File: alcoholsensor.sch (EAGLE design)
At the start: 23 parts, among them IC2 7805TV

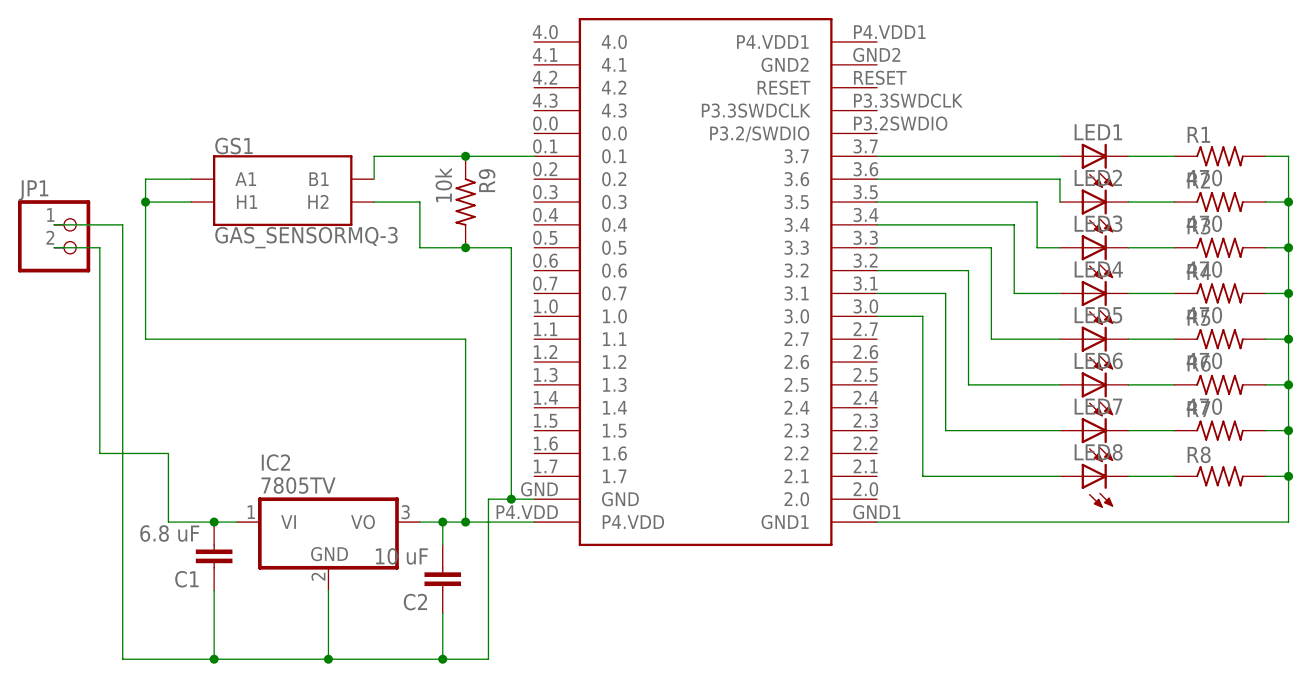
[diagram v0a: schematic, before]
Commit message: Improved design (made smaller)
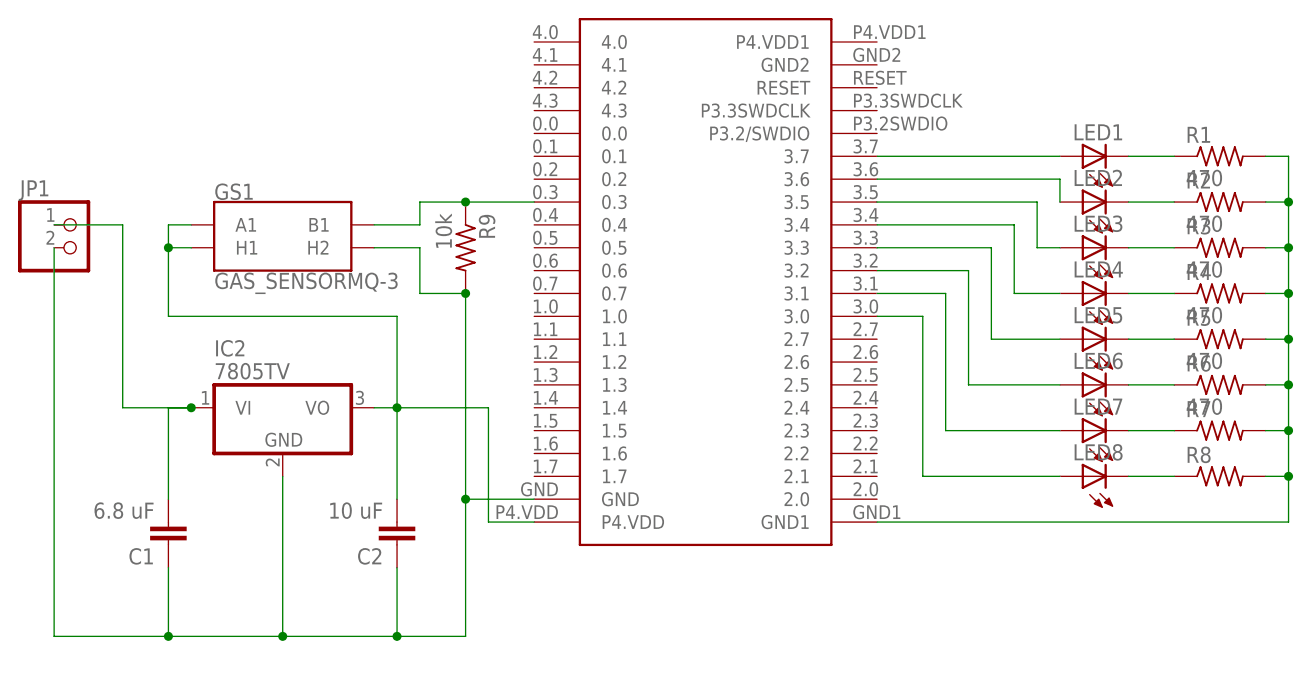
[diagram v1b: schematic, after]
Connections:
- removed net N$20 (its old number): GS1.B1, R9.1, U$1.0.1
- new net N$18: C1.2, IC2.VI, JP1.1
- net N$21: now also GS1.B1, R9.1, U$1.0.3; no longer C1.2, IC2.VI, JP1.2
- net N$22: now also JP1.2; no longer JP1.1
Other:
- moved on the sheet: C1, C2, GS1, IC2, R9
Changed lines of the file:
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@@
 <instance part="R7" gate="G$1" x="147.32" y="27.94"/>
 <instance part="R8" gate="G$1" x="147.32" y="22.86"/>
-<instance part="R9" gate="G$1" x="63.5" y="53.34" rot="R270"/>
+<instance part="R9" gate="G$1" x="63.5" y="48.26" rot="R270"/>
 <instance part="JP1" gate="G$1" x="20.32" y="48.26"/>
-<instance part="IC2" gate="A1" x="48.26" y="17.78"/>
-<instance part="C1" gate="G$1" x="35.56" y="12.7" rot="R180"/>
-<instance part="C2" gate="G$1" x="60.96" y="10.16" rot="R180"/>
-<instance part="GS1" gate="G$1" x="43.18" y="53.34"/>
+<instance part="IC2" gate="A1" x="43.18" y="30.48"/>
+<instance part="C1" gate="G$1" x="30.48" y="15.24" rot="R180"/>
+<instance part="C2" gate="G$1" x="55.88" y="15.24" rot="R180"/>
+<instance part="GS1" gate="G$1" x="43.18" y="48.26"/>
 </instances>
 <busses>
@@
 <net name="N$18" class="0">
 <segment>
+<pinref part="JP1" gate="G$1" pin="1"/>
+<wire x1="17.78" y1="50.8" x2="25.4" y2="50.8" width="0.1524" layer="91"/>
+<wire x1="25.4" y1="50.8" x2="25.4" y2="30.48" width="0.1524" layer="91"/>
+<pinref part="IC2" gate="A1" pin="VI"/>
+<wire x1="25.4" y1="30.48" x2="33.02" y2="30.48" width="0.1524" layer="91"/>
+<pinref part="C1" gate="G$1" pin="2"/>
+<wire x1="33.02" y1="30.48" x2="30.48" y2="30.48" width="0.1524" layer="91"/>
+<wire x1="30.48" y1="30.48" x2="30.48" y2="20.32" width="0.1524" layer="91"/>
+<junction x="33.02" y="30.48"/>
+</segment>
+</net>
+<net name="N$20" class="0">
+<segment>
+<pinref part="C2" gate="G$1" pin="2"/>
+<wire x1="55.88" y1="20.32" x2="55.88" y2="30.48" width="0.1524" layer="91"/>
+<pinref part="IC2" gate="A1" pin="VO"/>
+<wire x1="55.88" y1="30.48" x2="53.34" y2="30.48" width="0.1524" layer="91"/>
+<wire x1="66.04" y1="30.48" x2="66.04" y2="17.78" width="0.1524" layer="91"/>
+<junction x="55.88" y="30.48"/>
 <pinref part="U$1" gate="G$1" pin="P4.VDD"/>
-<wire x1="58.42" y1="17.78" x2="60.96" y2="17.78" width="0.1524" layer="91"/>
-<wire x1="60.96" y1="17.78" x2="63.5" y2="17.78" width="0.1524" layer="91"/>
-<wire x1="63.5" y1="17.78" x2="71.12" y2="17.78" width="0.1524" layer="91"/>
-<wire x1="63.5" y1="17.78" x2="63.5" y2="38.1" width="0.1524" layer="91"/>
-<junction x="63.5" y="17.78"/>
-<wire x1="63.5" y1="38.1" x2="27.94" y2="38.1" width="0.1524" layer="91"/>
-<wire x1="27.94" y1="38.1" x2="27.94" y2="53.34" width="0.1524" layer="91"/>
-<pinref part="IC2" gate="A1" pin="VO"/>
-<pinref part="C2" gate="G$1" pin="2"/>
-<wire x1="27.94" y1="53.34" x2="27.94" y2="55.88" width="0.1524" layer="91"/>
-<wire x1="60.96" y1="15.24" x2="60.96" y2="17.78" width="0.1524" layer="91"/>
-<junction x="60.96" y="17.78"/>
+<wire x1="66.04" y1="17.78" x2="71.12" y2="17.78" width="0.1524" layer="91"/>
+<wire x1="66.04" y1="30.48" x2="55.88" y2="30.48" width="0.1524" layer="91"/>
+<wire x1="55.88" y1="30.48" x2="55.88" y2="40.64" width="0.1524" layer="91"/>
+<wire x1="55.88" y1="40.64" x2="30.48" y2="40.64" width="0.1524" layer="91"/>
+<wire x1="30.48" y1="40.64" x2="30.48" y2="48.26" width="0.1524" layer="91"/>
+<pinref part="GS1" gate="G$1" pin="H1"/>
+<wire x1="30.48" y1="48.26" x2="33.02" y2="48.26" width="0.1524" layer="91"/>
 <pinref part="GS1" gate="G$1" pin="A1"/>
-<wire x1="27.94" y1="55.88" x2="33.02" y2="55.88" width="0.1524" layer="91"/>
-<pinref part="GS1" gate="G$1" pin="H1"/>
-<wire x1="27.94" y1="53.34" x2="33.02" y2="53.34" width="0.1524" layer="91"/>
-<junction x="27.94" y="53.34"/>
-</segment>
-</net>
-<net name="N$20" class="0">
-<segment>
+<wire x1="33.02" y1="50.8" x2="30.48" y2="50.8" width="0.1524" layer="91"/>
+<wire x1="30.48" y1="50.8" x2="30.48" y2="48.26" width="0.1524" layer="91"/>
+<junction x="30.48" y="48.26"/>
+</segment>
+</net>
+<net name="N$21" class="0">
+<segment>
+<pinref part="GS1" gate="G$1" pin="B1"/>
+<wire x1="53.34" y1="50.8" x2="58.42" y2="50.8" width="0.1524" layer="91"/>
+<wire x1="58.42" y1="50.8" x2="58.42" y2="53.34" width="0.1524" layer="91"/>
 <pinref part="R9" gate="G$1" pin="1"/>
-<pinref part="U$1" gate="G$1" pin="0.1"/>
-<wire x1="63.5" y1="58.42" x2="71.12" y2="58.42" width="0.1524" layer="91"/>
-<pinref part="GS1" gate="G$1" pin="B1"/>
-<wire x1="53.34" y1="55.88" x2="53.34" y2="58.42" width="0.1524" layer="91"/>
-<wire x1="53.34" y1="58.42" x2="63.5" y2="58.42" width="0.1524" layer="91"/>
-<junction x="63.5" y="58.42"/>
-</segment>
-</net>
-<net name="N$21" class="0">
-<segment>
-<wire x1="30.48" y1="25.4" x2="30.48" y2="17.78" width="0.1524" layer="91"/>
+<wire x1="58.42" y1="53.34" x2="63.5" y2="53.34" width="0.1524" layer="91"/>
+<pinref part="U$1" gate="G$1" pin="0.3"/>
+<wire x1="63.5" y1="53.34" x2="71.12" y2="53.34" width="0.1524" layer="91"/>
+<junction x="63.5" y="53.34"/>
+</segment>
+</net>
+<net name="N$22" class="0">
+<segment>
+<pinref part="GS1" gate="G$1" pin="H2"/>
+<wire x1="53.34" y1="48.26" x2="58.42" y2="48.26" width="0.1524" layer="91"/>
+<wire x1="58.42" y1="48.26" x2="58.42" y2="43.18" width="0.1524" layer="91"/>
+<pinref part="R9" gate="G$1" pin="2"/>
+<wire x1="58.42" y1="43.18" x2="63.5" y2="43.18" width="0.1524" layer="91"/>
 <pinref part="JP1" gate="G$1" pin="2"/>
-<wire x1="17.78" y1="48.26" x2="22.86" y2="48.26" width="0.1524" layer="91"/>
-<wire x1="22.86" y1="48.26" x2="22.86" y2="25.4" width="0.1524" layer="91"/>
-<wire x1="22.86" y1="25.4" x2="30.48" y2="25.4" width="0.1524" layer="91"/>
-<pinref part="IC2" gate="A1" pin="VI"/>
-<pinref part="C1" gate="G$1" pin="2"/>
-<wire x1="38.1" y1="17.78" x2="35.56" y2="17.78" width="0.1524" layer="91"/>
-<wire x1="30.48" y1="17.78" x2="35.56" y2="17.78" width="0.1524" layer="91"/>
-<junction x="35.56" y="17.78"/>
-</segment>
-</net>
-<net name="N$22" class="0">
-<segment>
-<wire x1="48.26" y1="10.16" x2="48.26" y2="2.54" width="0.1524" layer="91"/>
-<wire x1="48.26" y1="2.54" x2="60.96" y2="2.54" width="0.1524" layer="91"/>
-<wire x1="60.96" y1="2.54" x2="66.04" y2="2.54" width="0.1524" layer="91"/>
-<wire x1="66.04" y1="2.54" x2="66.04" y2="20.32" width="0.1524" layer="91"/>
-<junction x="48.26" y="2.54"/>
+<wire x1="17.78" y1="48.26" x2="17.78" y2="5.08" width="0.1524" layer="91"/>
+<wire x1="17.78" y1="5.08" x2="30.48" y2="5.08" width="0.1524" layer="91"/>
+<pinref part="IC2" gate="A1" pin="GND"/>
+<wire x1="30.48" y1="5.08" x2="43.18" y2="5.08" width="0.1524" layer="91"/>
+<wire x1="43.18" y1="5.08" x2="43.18" y2="22.86" width="0.1524" layer="91"/>
+<pinref part="C1" gate="G$1" pin="1"/>
+<wire x1="30.48" y1="12.7" x2="30.48" y2="5.08" width="0.1524" layer="91"/>
+<junction x="30.48" y="5.08"/>
+<pinref part="C2" gate="G$1" pin="1"/>
+<wire x1="55.88" y1="12.7" x2="55.88" y2="5.08" width="0.1524" layer="91"/>
+<wire x1="55.88" y1="5.08" x2="43.18" y2="5.08" width="0.1524" layer="91"/>
+<junction x="43.18" y="5.08"/>
+<wire x1="55.88" y1="5.08" x2="63.5" y2="5.08" width="0.1524" layer="91"/>
+<wire x1="63.5" y1="5.08" x2="63.5" y2="20.32" width="0.1524" layer="91"/>
+<junction x="55.88" y="5.08"/>
 <pinref part="U$1" gate="G$1" pin="GND"/>
-<wire x1="66.04" y1="20.32" x2="68.58" y2="20.32" width="0.1524" layer="91"/>
-<wire x1="68.58" y1="20.32" x2="71.12" y2="20.32" width="0.1524" layer="91"/>
-<pinref part="R9" gate="G$1" pin="2"/>
-<wire x1="58.42" y1="48.26" x2="63.5" y2="48.26" width="0.1524" layer="91"/>
-<wire x1="63.5" y1="48.26" x2="68.58" y2="48.26" width="0.1524" layer="91"/>
-<wire x1="68.58" y1="48.26" x2="68.58" y2="20.32" width="0.1524" layer="91"/>
-<junction x="63.5" y="48.26"/>
-<junction x="68.58" y="20.32"/>
-<wire x1="48.26" y1="2.54" x2="35.56" y2="2.54" width="0.1524" layer="91"/>
-<wire x1="35.56" y1="2.54" x2="25.4" y2="2.54" width="0.1524" layer="91"/>
-<wire x1="25.4" y1="2.54" x2="25.4" y2="50.8" width="0.1524" layer="91"/>
-<pinref part="JP1" gate="G$1" pin="1"/>
-<wire x1="25.4" y1="50.8" x2="17.78" y2="50.8" width="0.1524" layer="91"/>
-<pinref part="IC2" gate="A1" pin="GND"/>
-<pinref part="C1" gate="G$1" pin="1"/>
-<wire x1="35.56" y1="10.16" x2="35.56" y2="2.54" width="0.1524" layer="91"/>
-<junction x="35.56" y="2.54"/>
-<pinref part="C2" gate="G$1" pin="1"/>
-<wire x1="60.96" y1="7.62" x2="60.96" y2="2.54" width="0.1524" layer="91"/>
-<junction x="60.96" y="2.54"/>
-<pinref part="GS1" gate="G$1" pin="H2"/>
-<wire x1="53.34" y1="53.34" x2="58.42" y2="53.34" width="0.1524" layer="91"/>
-<wire x1="58.42" y1="53.34" x2="58.42" y2="48.26" width="0.1524" layer="91"/>
-</segment>
-</net>
+<wire x1="63.5" y1="20.32" x2="71.12" y2="20.32" width="0.1524" layer="91"/>
+<wire x1="63.5" y1="43.18" x2="63.5" y2="20.32" width="0.1524" layer="91"/>
+<junction x="63.5" y="43.18"/>
+<junction x="63.5" y="20.32"/>
+</segment>
+</net>

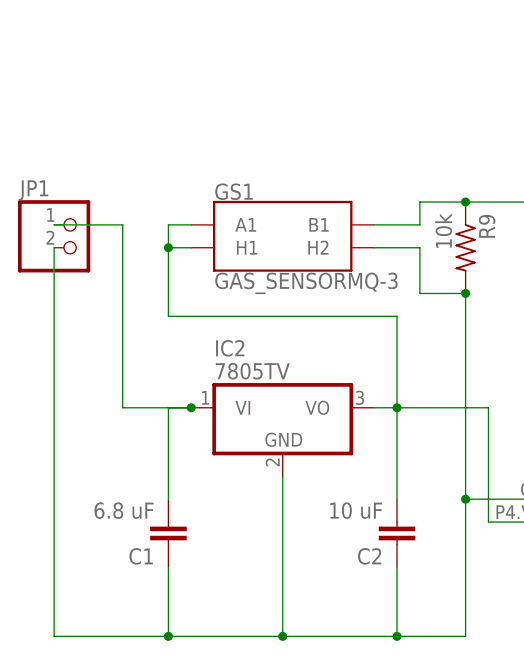
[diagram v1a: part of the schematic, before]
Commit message: Added pushbutton switch to control power source
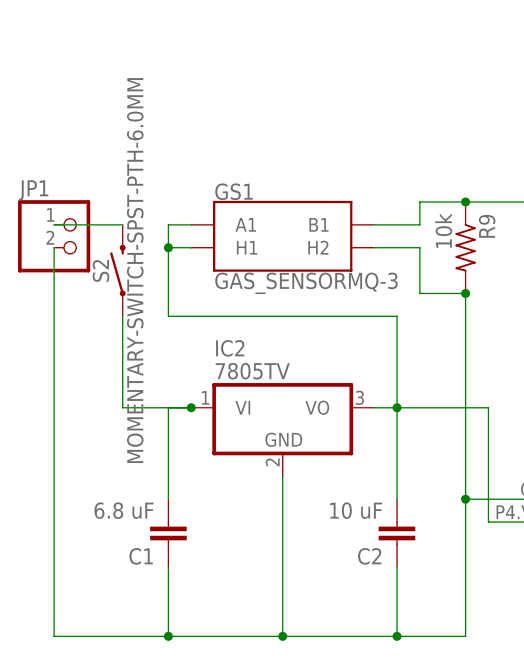
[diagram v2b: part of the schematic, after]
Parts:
- added S2: MOMENTARY-SWITCH-SPST-PTH-6.0MM, SparkFun-Switches:MOMENTARY-SWITCH-SPST-PTH-6.0MM
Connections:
- net N$1 renamed RED
- net N$17 renamed GND2
- net N$2 renamed RED1
- net N$20 renamed 5V
- net N$21 renamed DATA
- net N$22 renamed GND1
- net N$3 renamed ORANGE
- net N$4 renamed ORANGE1
- net N$5 renamed GREEN
- net N$6 renamed GREEN1
- net N$7 renamed BLUE
- net N$8 renamed BLUE1
- removed net N$18: C1.2, IC2.VI, JP1.1
- new net 6V: C1.2, IC2.VI, S2.1
- new net N$1: JP1.1, S2.2
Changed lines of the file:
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@@
 <part name="C2" library="capacitor-wima" deviceset="C" device="2.5/4" value="10 uF"/>
 <part name="GS1" library="SparkFun-Sensors" deviceset="GAS_SENSOR" device="MQ-3"/>
+<part name="S2" library="SparkFun-Switches" deviceset="MOMENTARY-SWITCH-SPST" device="-PTH-6.0MM"/>
 </parts>
 <sheets>
@@
 <instance part="C2" gate="G$1" x="55.88" y="15.24" rot="R180"/>
 <instance part="GS1" gate="G$1" x="43.18" y="48.26"/>
+<instance part="S2" gate="G$1" x="25.4" y="45.72" rot="R90"/>
 </instances>
 <busses>
 </busses>
 <nets>
-<net name="N$1" class="0">
+<net name="RED" class="0">
 <segment>
 <pinref part="U$1" gate="G$1" pin="3.7"/>
@@
 </segment>
 </net>
-<net name="N$2" class="0">
+<net name="RED1" class="0">
 <segment>
 <pinref part="U$1" gate="G$1" pin="3.6"/>
@@
 </segment>
 </net>
-<net name="N$3" class="0">
+<net name="ORANGE" class="0">
 <segment>
 <pinref part="U$1" gate="G$1" pin="3.5"/>
@@
 </segment>
 </net>
-<net name="N$4" class="0">
+<net name="ORANGE1" class="0">
 <segment>
 <pinref part="U$1" gate="G$1" pin="3.4"/>
@@
 </segment>
 </net>
-<net name="N$5" class="0">
+<net name="GREEN" class="0">
 <segment>
 <pinref part="U$1" gate="G$1" pin="3.3"/>
@@
 </segment>
 </net>
-<net name="N$6" class="0">
+<net name="GREEN1" class="0">
 <segment>
 <pinref part="U$1" gate="G$1" pin="3.2"/>
@@
 </segment>
 </net>
-<net name="N$7" class="0">
+<net name="BLUE" class="0">
 <segment>
 <pinref part="U$1" gate="G$1" pin="3.1"/>
@@
 </segment>
 </net>
-<net name="N$8" class="0">
+<net name="BLUE1" class="0">
 <segment>
 <pinref part="U$1" gate="G$1" pin="3.0"/>
@@
 </segment>
 </net>
-<net name="N$17" class="0">
+<net name="GND2" class="0">
 <segment>
 <pinref part="R8" gate="G$1" pin="2"/>
@@
 </segment>
 </net>
-<net name="N$18" class="0">
-<segment>
-<pinref part="JP1" gate="G$1" pin="1"/>
-<wire x1="17.78" y1="50.8" x2="25.4" y2="50.8" width="0.1524" layer="91"/>
-<wire x1="25.4" y1="50.8" x2="25.4" y2="30.48" width="0.1524" layer="91"/>
+<net name="6V" class="0">
+<segment>
 <pinref part="IC2" gate="A1" pin="VI"/>
 <wire x1="25.4" y1="30.48" x2="33.02" y2="30.48" width="0.1524" layer="91"/>
@@
 <wire x1="30.48" y1="30.48" x2="30.48" y2="20.32" width="0.1524" layer="91"/>
 <junction x="33.02" y="30.48"/>
-</segment>
-</net>
-<net name="N$20" class="0">
+<pinref part="S2" gate="G$1" pin="1"/>
+<wire x1="25.4" y1="40.64" x2="25.4" y2="30.48" width="0.1524" layer="91"/>
+</segment>
+</net>
+<net name="5V" class="0">
 <segment>
 <pinref part="C2" gate="G$1" pin="2"/>
@@
 </segment>
 </net>
-<net name="N$21" class="0">
+<net name="DATA" class="0">
 <segment>
 <pinref part="GS1" gate="G$1" pin="B1"/>
@@
 </segment>
 </net>
-<net name="N$22" class="0">
+<net name="GND1" class="0">
 <segment>
 <pinref part="GS1" gate="G$1" pin="H2"/>
@@
 </segment>
 </net>
+<net name="N$1" class="0">
+<segment>
+<pinref part="JP1" gate="G$1" pin="1"/>
+<pinref part="S2" gate="G$1" pin="2"/>
+<wire x1="17.78" y1="50.8" x2="25.4" y2="50.8" width="0.1524" layer="91"/>
+</segment>
+</net>
